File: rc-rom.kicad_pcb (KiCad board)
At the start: 2 copper layers, 99.1 x 49.9 mm, 21 parts, among them J1 RC2014, J2 RC2014_Enh, U1 27C512, U2 74HCT138, U3 74HCT74, U4 74HCT4075

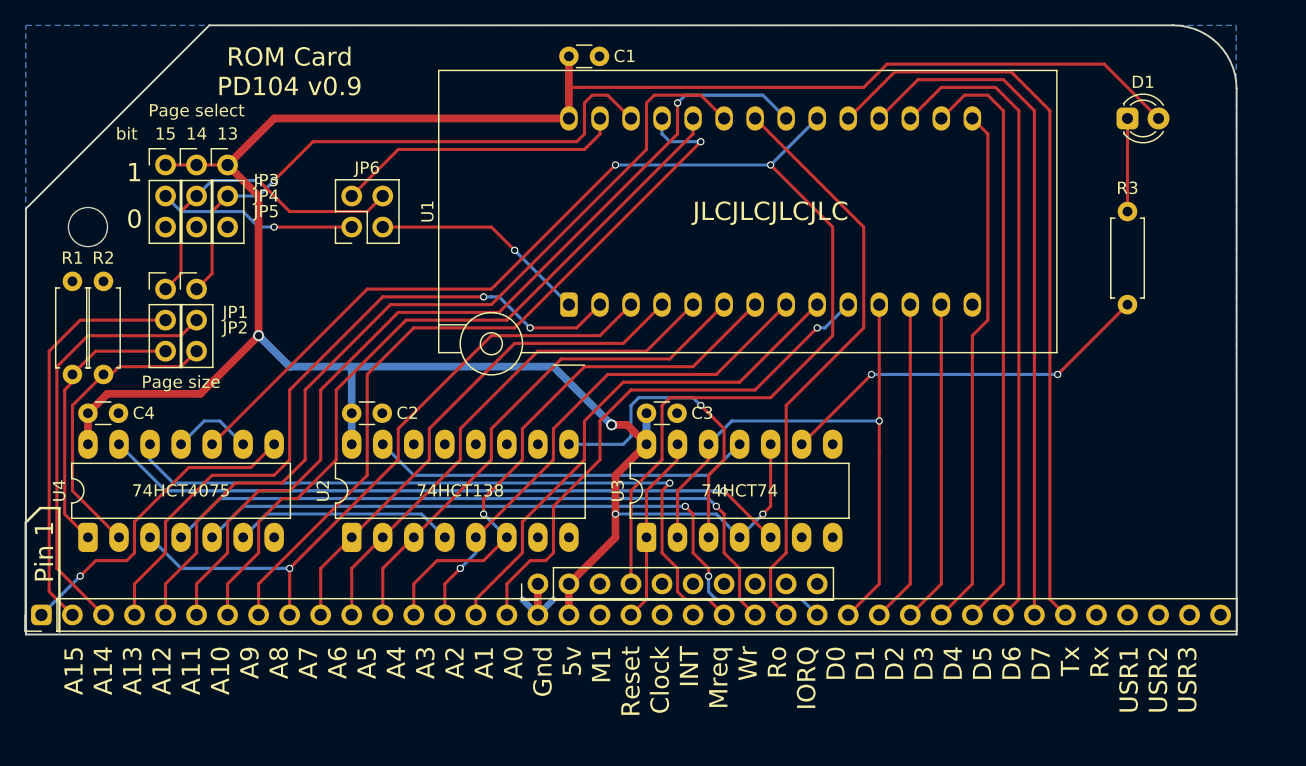
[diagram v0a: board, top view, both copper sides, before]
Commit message: Added silkscreen jumper diagrams, tweaked net labels
Added reference diagrams for jumpers on the silkscreen, tweaked net labels
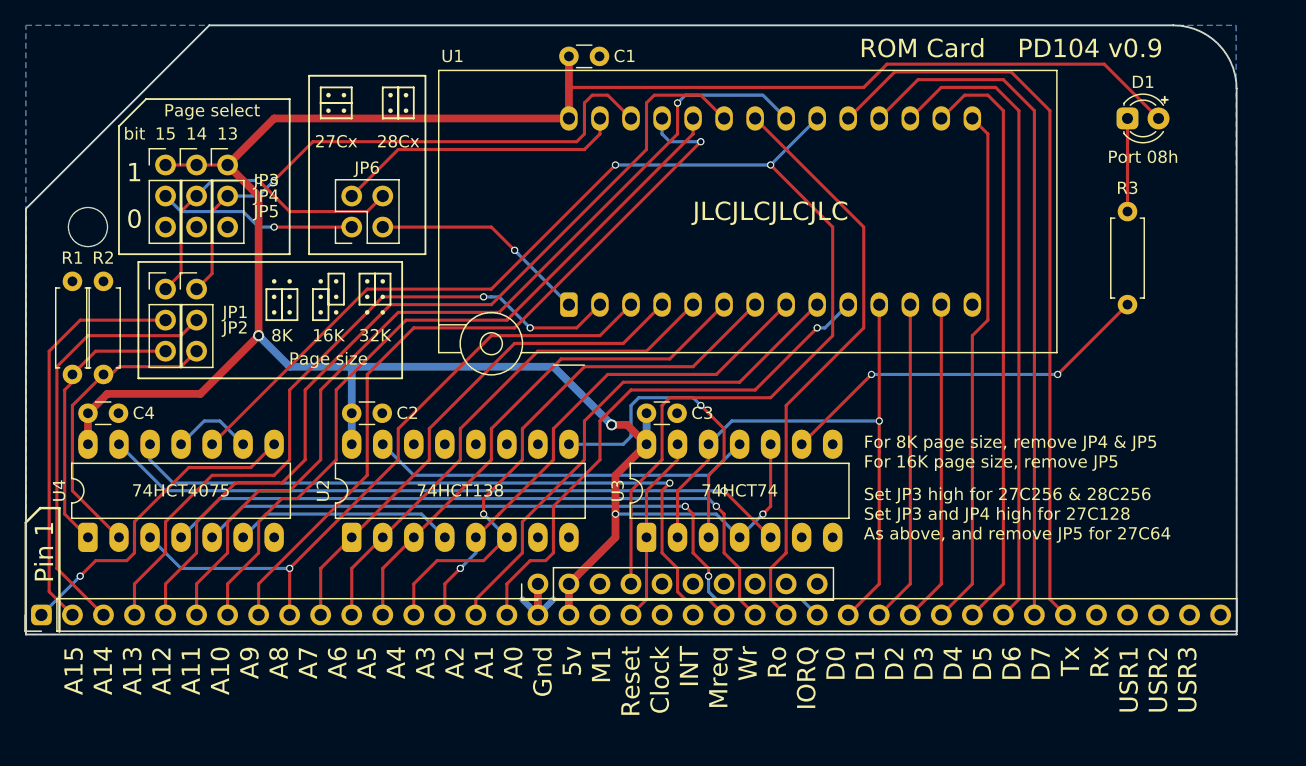
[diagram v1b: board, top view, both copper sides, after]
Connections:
- net /LED renamed /~LED
- net /ROM_A14S renamed /ROM_A14'
- net /ROM_A15S renamed /ROM_A15'
- net Net-(D1-Pad1) renamed /~LED'
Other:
- board text added: "16K"
- board text added: "27Cx"
- board text added: "28Cx"
- board text added: "32K"
- board text added: "8K"
- board text added: "For 8K page size, remove JP4 & JP5 For 16K page size, remove JP5"
- board text added: "Port 08h"
- board text added: "Set JP3 high for 27C256 & 28C256 Set JP3 and JP4 high for 27C128 As above, and remove JP5 for 27C64"

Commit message: Fix silk instructions
Whoops the jumper instructions on the silk were wrong
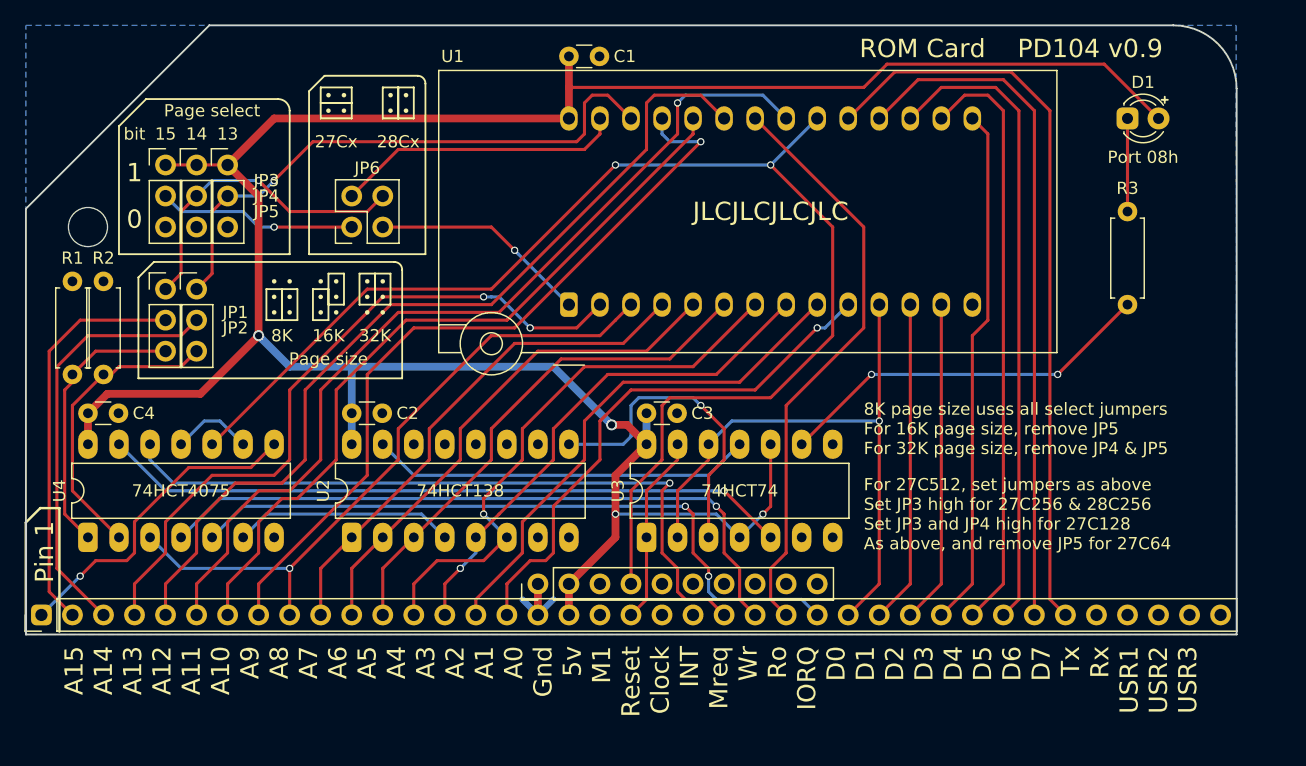
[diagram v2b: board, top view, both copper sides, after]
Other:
- board text added: "8K page size uses all select jumpers For 16K page size, remove JP5 For 32K page size, remove JP4 & JP5"
- board text added: "For 27C512, set jumpers as above Set JP3 high for 27C256 & 28C256 Set JP3 and JP4 high for 27C128 As above, and remove JP5 for 27C64"
- board text removed: "For 8K page size, remove JP4 & JP5 For 16K page size, remove JP5"
- board text removed: "Set JP3 high for 27C256 & 28C256 Set JP3 and JP4 high for 27C128 As above, and remove JP5 for 27C64"

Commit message: Added README, tidied up schematic and board
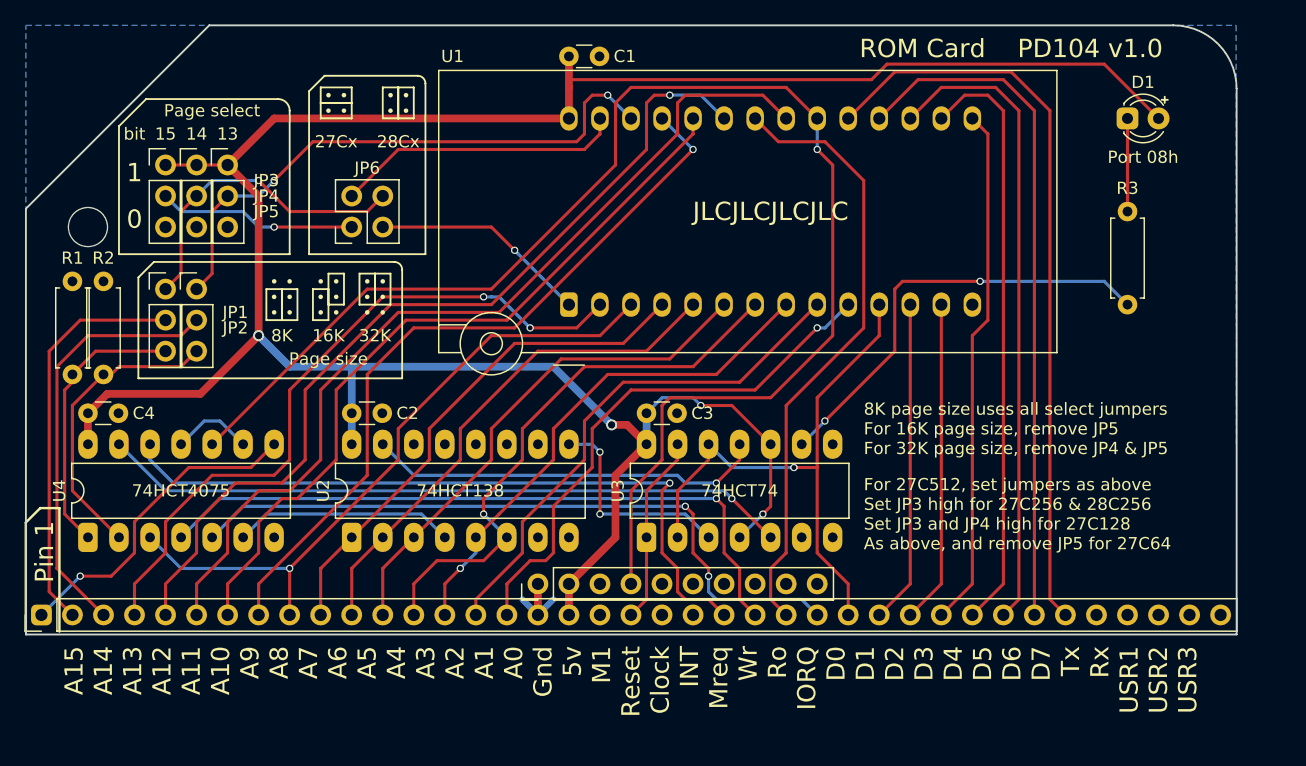
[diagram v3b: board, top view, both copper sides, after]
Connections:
- net /~ROM_EN renamed ~ROM_EN
- net ~ROM_CS renamed /~ROM_CS
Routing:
- net /~ROM_CFG: track 26.2 -> 17.6 mm, vias 1 -> 2
- net PAGE: track 108.6 -> 116.0 mm, vias 2 -> 1
- net /~LED: track 31.4 -> 36.0 mm
- net D0: track 49.9 -> 46.9 mm
- net ~RD: track 48.0 -> 50.2 mm
- net A8: track 63.3 -> 61.3 mm
- net /~LED_CFG: track 31.6 -> 32.9 mm, vias 0 -> 1
- net +5V: track 205.3 -> 206.3 mm
- net A11: vias 0 -> 1
- net ROM_A13: vias 1 -> 2
- net A10: vias 1 -> 0
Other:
- board text added: "ROM Card PD104 v1.0"
- board text removed: "ROM Card PD104 v0.9"

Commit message: Moved to version 1.1, added LED for paging status
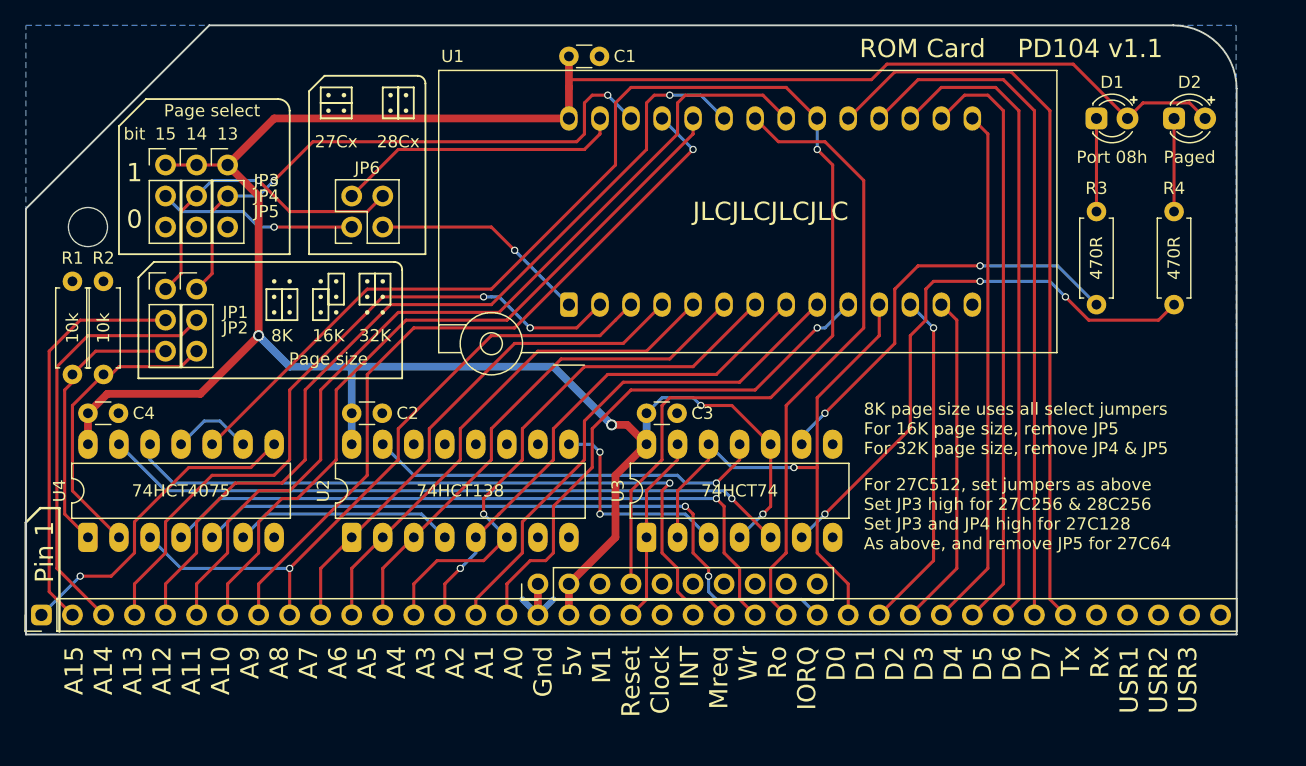
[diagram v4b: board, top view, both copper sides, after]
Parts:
- added D2: Green, LED_THT:LED_D3.0mm, F.Cu at (246.4, 109.2)
- added R4: 470R, Resistor_THT:R_Axial_DIN0207_L6.3mm_D2.5mm_P7.62mm_Horizontal, F.Cu at (246.4, 124.5)
- D1: value LED -> Yellow
- moved D1 2.54 mm to (240.0, 109.2)
- moved R3 2.54 mm to (240.0, 116.8)
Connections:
- U3 pad 6: Net-(U3-Pad6) -> /~Paged
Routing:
- net /~Paged: track 0.00 -> 47.0 mm, vias 0 -> 3
- net /~Paged': track 0.00 -> 7.62 mm
- net +5V: track 206.3 -> 211.2 mm
- net D1: track 26.5 -> 28.0 mm, vias 0 -> 1
- net /~LED: track 36.0 -> 34.5 mm
- net D2: track 26.5 -> 27.5 mm
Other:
- board text added: "Paged"
- board text added: "ROM Card PD104 v1.1"
- board text removed: "ROM Card PD104 v1.0"

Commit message: Update silkscreen
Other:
- board text added: "27C512: Set jumpers as above 27C256 & 28C256: Set bit 15 high 27C128: Set bits 15 and 14 high 27C64: As above, and remove bit 13 28C64: Set 15 high, remove 13 & 14"
- board text added: "Notes for page select jumpers: 8K page size uses all select jumpers For 16K pages, remove bit 13 For 32K pages, remove bits 13 & 14"
- board text removed: "8K page size uses all select jumpers For 16K page size, remove JP5 For 32K page size, remove JP4 & JP5"
- board text removed: "For 27C512, set jumpers as above Set JP3 high for 27C256 & 28C256 Set JP3 and JP4 high for 27C128 As above, and remove JP5 for 27C64"
